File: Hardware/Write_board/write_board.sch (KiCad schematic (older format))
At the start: 57 parts

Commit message: erc
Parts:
- gave numbers to parts that had none: 48
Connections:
- net !RST: now also U4.6 (OUT); no longer U4.3 (OUT)
- net GND: now also P1.2 (P2), P5.2 (P2), U9.12, U9.13, U9.4, U9.5; no longer U9.12, U9.13, U9.4, U9.5
- net GW: now also U9.3
- net PB1deb: now also U4.1 (IN1)
- net RST: now also U4.5 (IN2); no longer U4.2 (IN2)
- net VCC: now also U4.4 (IN1); no longer U4.1 (IN1)
- no-connect marks 5 -> 25

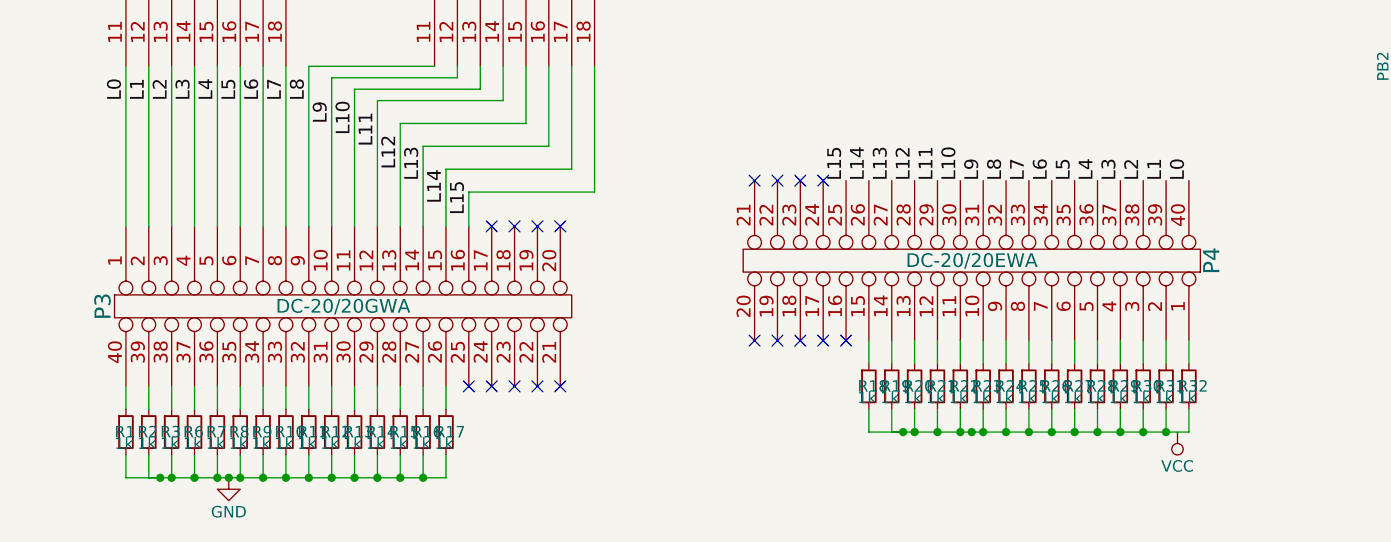
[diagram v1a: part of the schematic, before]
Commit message: Connector correction
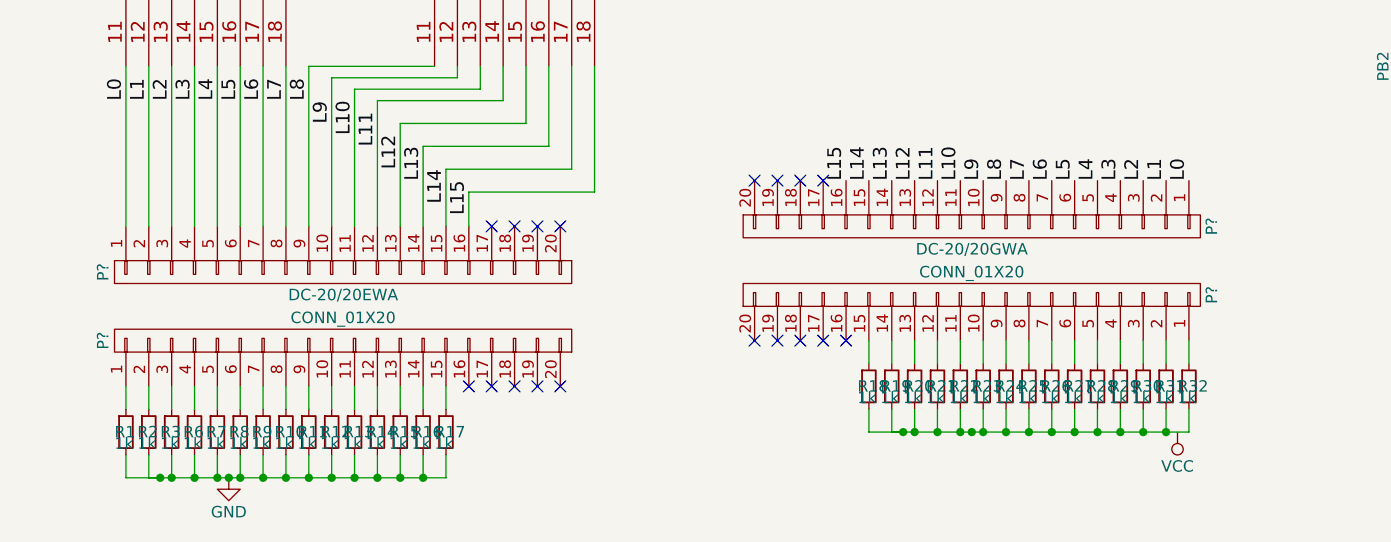
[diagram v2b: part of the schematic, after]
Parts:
- removed P3: DC-20/20GWA, symbol DIL40
- removed P4: DC-20/20EWA, symbol DIL40
- added P?: DC-20/20EWA, symbol CONN_01X20
- added P? (x2): CONN_01X20, symbol CONN_01X20
- added P?: DC-20/20GWA, symbol CONN_01X20
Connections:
- net L0: now also P?.1 (P1), P?.1 (P1)
- net L1: now also P?.2 (P2), P?.2 (P2)
- net L10: now also P?.11 (P11), P?.11 (P11)
- net L11: now also P?.12 (P12), P?.12 (P12)
- net L12: now also P?.13 (P13), P?.13 (P13)
- net L13: now also P?.14 (P14), P?.14 (P14)
- net L14: now also P?.15 (P15), P?.15 (P15)
- net L15: now also P?.16 (P16), P?.16 (P16)
- net L2: now also P?.3 (P3), P?.3 (P3)
- net L3: now also P?.4 (P4), P?.4 (P4)
- net L4: now also P?.5 (P5), P?.5 (P5)
- net L5: now also P?.6 (P6), P?.6 (P6)
- net L6: now also P?.7 (P7), P?.7 (P7)
- net L7: now also P?.8 (P8), P?.8 (P8)
- net L8: now also P?.9 (P9), P?.9 (P9)
- net L9: now also P?.10 (P10), P?.10 (P10)
- net at R17.1: now also P?.15 (P15)
- net at R16.1: now also P?.14 (P14)
- net at R15.1: now also P?.13 (P13)
- net at R14.1: now also P?.12 (P12)
- net at R13.1: now also P?.11 (P11)
- net at R12.1: now also P?.10 (P10)
- net at R11.1: now also P?.9 (P9)
- net at R10.1: now also P?.8 (P8)
- net at R9.1: now also P?.7 (P7)
- net at R8.1: now also P?.6 (P6)
- net at R7.1: now also P?.5 (P5)
- net at R6.1: now also P?.4 (P4)
- net at R3.1: now also P?.3 (P3)
- net at R2.1: now also P?.2 (P2)
- net at R1.1: now also P?.1 (P1)
- net at R32.1: now also P?.1 (P1)
- net at R23.1: now also P?.10 (P10)
- net at R22.1: now also P?.11 (P11)
- net at R21.1: now also P?.12 (P12)
- net at R20.1: now also P?.13 (P13)
- net at R19.1: now also P?.14 (P14)
- net at R18.1: now also P?.15 (P15)
- net at R31.1: now also P?.2 (P2)
- net at R30.1: now also P?.3 (P3)
- net at R29.1: now also P?.4 (P4)
- net at R28.1: now also P?.5 (P5)
- net at R27.1: now also P?.6 (P6)
- net at R26.1: now also P?.7 (P7)
- net at R25.1: now also P?.8 (P8)
- net at R24.1: now also P?.9 (P9)
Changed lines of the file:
@@
 NoConn ~ 10250 5300
-$Comp
-L DIL40 P3
-U 1 1 5623B91B
-P 2300 6850
-F 0 "P3" H 2300 7900 70  0000 C CNN
-F 1 "DC-20/20GWA" V 2300 6850 60  0000 C CNN
-F 2 "" H 2300 6850 60  0000 C CNN
-F 3 "" H 2300 6850 60  0000 C CNN
-	1    2300 6850
-	0    -1   1    0
-$EndComp
-$Comp
-L DIL40 P4
-U 1 1 5623BA80
-P 5050 6650
-F 0 "P4" H 5050 7700 70  0000 C CNN
-F 1 "DC-20/20EWA" V 5050 6650 60  0000 C CNN
-F 2 "" H 5050 6650 60  0000 C CNN
-F 3 "" H 5050 6650 60  0000 C CNN
-	1    5050 6650
-	0    1    -1   0
-$EndComp
 $Comp
 L 74LS541 U1
@@
 	2350 2250 2350 2150
 Connection ~ 2350 2150
+$Comp
+L CONN_01X20 P?
+U 1 1 5624C5FF
+P 2300 6700
+F 0 "P?" H 2300 7750 50  0000 C CNN
+F 1 "DC-20/20EWA" V 2400 6700 50  0000 C CNN
+F 2 "" H 2300 6700 60  0000 C CNN
+F 3 "" H 2300 6700 60  0000 C CNN
+	1    2300 6700
+	0    -1   1    0
+$EndComp
+$Comp
+L CONN_01X20 P?
+U 1 1 5624C7E9
+P 2300 7000
+F 0 "P?" H 2300 8050 50  0000 C CNN
+F 1 "CONN_01X20" V 2400 7000 50  0000 C CNN
+F 2 "" H 2300 7000 60  0000 C CNN
+F 3 "" H 2300 7000 60  0000 C CNN
+	1    2300 7000
+	0    -1   -1   0
+$EndComp
+$Comp
+L CONN_01X20 P?
+U 1 1 5624CC48
+P 5050 6500
+F 0 "P?" H 5050 7550 50  0000 C CNN
+F 1 "DC-20/20GWA" V 5150 6500 50  0000 C CNN
+F 2 "" H 5050 6500 60  0000 C CNN
+F 3 "" H 5050 6500 60  0000 C CNN
+	1    5050 6500
+	0    1    1    0
+$EndComp
+$Comp
+L CONN_01X20 P?
+U 1 1 5624CCEC
+P 5050 6800
+F 0 "P?" H 5050 7850 50  0000 C CNN
+F 1 "CONN_01X20" V 5150 6800 50  0000 C CNN
+F 2 "" H 5050 6800 60  0000 C CNN
+F 3 "" H 5050 6800 60  0000 C CNN
+	1    5050 6800
+	0    1    -1   0
+$EndComp
 $EndSCHEMATC
